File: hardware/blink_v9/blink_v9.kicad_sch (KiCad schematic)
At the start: 121 parts, among them J1 Conn_01x02, J14 Conn_02x16_Odd_Even, J15 Conn_01x01, J16 Conn_01x01, J5 Conn_01x06_Pin, J6 Conn_01x03, J7 Conn_01x06_Pin, J9 USB_C_Receptacle, Q1 S8550, Q2 S8050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

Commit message: add temp sensor
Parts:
- added C30: 100n, Capacitor_SMD:C_0402_1005Metric, symbol Device:C_Small
- added U10: TMP102xxDRL, Package_TO_SOT_SMD:SOT-563, symbol Sensor_Temperature:TMP102xxDRL
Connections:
- net +3.3V: now also C30.2, U10.5 (V+)
- net GND: now also C30.1, U10.2 (GND), U10.4 (ADD0)
- net SDA: now also U10.6 (SDA)
- new net SDL: U10.1 (SCL)
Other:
- note added: "I2C Addr: 0x48 (7bit)"
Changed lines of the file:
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@@
     (stroke (width 0) (type default))
   )
+  (text "I2C Addr: 0x48 (7bit)" (at 360.68 134.62 0)
+    (effects (font (size 1.27 1.27)) (justify left bottom))
+  )
   (text "To iPhone" (at 20.32 184.15 0)
     (effects (font (size 1.27 1.27)) (justify left bottom))
@@
     (effects (font (size 1.27 1.27)) (justify left bottom))
   )
+  (label "SDL" (at 358.14 142.24 180) (fields_autoplaced)
+    (effects (font (size 1.27 1.27)) (justify right bottom))
+  )
   (label "MON_PPS" (at 266.7 46.99 0) (fields_autoplaced)
     (effects (font (size 1.27 1.27)) (justify left bottom))
@@
     (effects (font (size 1.27 1.27)) (justify left bottom))
   )
+  (label "SDA" (at 358.14 139.7 180) (fields_autoplaced)
+    (effects (font (size 1.27 1.27)) (justify right bottom))
+  )
   (global_label "AUX_SYNC_IN" (shape input) (at 287.02 217.17 0) (fields_autoplaced)
     (effects (font (size 1.27 1.27)) (justify left))
@@
     )
   )
+  (symbol (lib_id "Sensor_Temperature:TMP102xxDRL") (at 368.3 144.78 0) (unit 1)
+    (in_bom yes) (on_board yes) (dnp no)
+    (property "Reference" "U10" (at 367.03 144.78 0)
+      (effects (font (size 1.27 1.27)))
+    )
+    (property "Value" "TMP102xxDRL" (at 368.3 154.94 0)
+      (effects (font (size 1.27 1.27)))
+    )
+    (property "Footprint" "Package_TO_SOT_SMD:SOT-563" (at 369.57 153.67 0)
+      (effects (font (size 1.27 1.27)) (justify left) hide)
+    )
+    (property "Datasheet" "https://www.ti.com/lit/ds/symlink/tmp102.pdf" (at 369.57 156.21 0)
+      (effects (font (size 1.27 1.27)) (justify left) hide)
+    )
+    (pin "1")
+    (pin "2")
+    (pin "3")
+    (pin "4")
+    (pin "5")
+    (pin "6")
+    (instances
+      (project "blink_v9"
+        (path "/bd4d3b9a-07c1-4a53-9c94-2893f3e869d4"
+          (reference "U10") (unit 1)
+        )
+      )
+    )
+  )
   (symbol (lib_id "power:GND") (at 163.83 53.34 0) (unit 1)
     (in_bom yes) (on_board yes) (dnp no) (fields_autoplaced)
@@
     )
   )
+  (symbol (lib_id "power:GND") (at 346.71 147.32 0) (unit 1)
+    (in_bom yes) (on_board yes) (dnp no)
+    (property "Reference" "#PWR025" (at 346.71 153.67 0)
+      (effects (font (size 1.27 1.27)) hide)
+    )
+    (property "Value" "GND" (at 346.71 152.4 0)
+      (effects (font (size 1.27 1.27)))
+    )
+    (property "Footprint" "" (at 346.71 147.32 0)
+      (effects (font (size 1.27 1.27)) hide)
+    )
+    (property "Datasheet" "" (at 346.71 147.32 0)
+      (effects (font (size 1.27 1.27)) hide)
+    )
+    (pin "1")
+    (instances
+      (project "blink_v9"
+        (path "/bd4d3b9a-07c1-4a53-9c94-2893f3e869d4"
+          (reference "#PWR025") (unit 1)
+        )
+      )
+    )
+  )
   (symbol (lib_id "power:PWR_FLAG") (at 66.04 45.72 0) (unit 1)
     (in_bom yes) (on_board yes) (dnp no) (fields_autoplaced)
@@
     )
   )
+  (symbol (lib_id "power:+3.3V") (at 368.3 134.62 0) (unit 1)
+    (in_bom yes) (on_board yes) (dnp no) (fields_autoplaced)
+    (property "Reference" "#PWR088" (at 368.3 138.43 0)
+      (effects (font (size 1.27 1.27)) hide)
+    )
+    (property "Value" "+3.3V" (at 368.3 129.54 0)
+      (effects (font (size 1.27 1.27)))
+    )
+    (property "Footprint" "" (at 368.3 134.62 0)
+      (effects (font (size 1.27 1.27)) hide)
+    )
+    (property "Datasheet" "" (at 368.3 134.62 0)
+      (effects (font (size 1.27 1.27)) hide)
+    )
+    (pin "1")
+    (instances
+      (project "blink_v9"
+        (path "/bd4d3b9a-07c1-4a53-9c94-2893f3e869d4"
+          (reference "#PWR088") (unit 1)
+        )
+      )
+    )
+  )
   (symbol (lib_id "power:GND") (at 227.33 219.71 0) (unit 1)
     (in_bom yes) (on_board yes) (dnp no) (fields_autoplaced)
@@
     )
   )
+  (symbol (lib_id "power:GND") (at 368.3 154.94 0) (unit 1)
+    (in_bom yes) (on_board yes) (dnp no)
+    (property "Reference" "#PWR024" (at 368.3 161.29 0)
+      (effects (font (size 1.27 1.27)) hide)
+    )
+    (property "Value" "GND" (at 368.3 160.02 0)
+      (effects (font (size 1.27 1.27)))
+    )
+    (property "Footprint" "" (at 368.3 154.94 0)
+      (effects (font (size 1.27 1.27)) hide)
+    )
+    (property "Datasheet" "" (at 368.3 154.94 0)
+      (effects (font (size 1.27 1.27)) hide)
+    )
+    (pin "1")
+    (instances
+      (project "blink_v9"
+        (path "/bd4d3b9a-07c1-4a53-9c94-2893f3e869d4"
+          (reference "#PWR024") (unit 1)
+        )
+      )
+    )
+  )
   (symbol (lib_id "Mechanical:MountingHole") (at 118.11 54.61 0) (unit 1)
     (in_bom no) (on_board yes) (dnp yes) (fields_autoplaced)
@@
     )
   )
+  (symbol (lib_id "power:GND") (at 358.14 147.32 0) (unit 1)
+    (in_bom yes) (on_board yes) (dnp no)
+    (property "Reference" "#PWR090" (at 358.14 153.67 0)
+      (effects (font (size 1.27 1.27)) hide)
+    )
+    (property "Value" "GND" (at 358.14 152.4 0)
+      (effects (font (size 1.27 1.27)))
+    )
+    (property "Footprint" "" (at 358.14 147.32 0)
+      (effects (font (size 1.27 1.27)) hide)
+    )
+    (property "Datasheet" "" (at 358.14 147.32 0)
+      (effects (font (size 1.27 1.27)) hide)
+    )
+    (pin "1")
+    (instances
+      (project "blink_v9"
+        (path "/bd4d3b9a-07c1-4a53-9c94-2893f3e869d4"
+          (reference "#PWR090") (unit 1)
+        )
+      )
+    )
+  )
   (symbol (lib_id "power:+3.3VA") (at 300.99 96.52 0) (unit 1)
     (in_bom yes) (on_board yes) (dnp no) (fields_autoplaced)
@@
     )
   )
+  (symbol (lib_id "power:+3.3V") (at 346.71 142.24 0) (unit 1)
+    (in_bom yes) (on_board yes) (dnp no) (fields_autoplaced)
+    (property "Reference" "#PWR089" (at 346.71 146.05 0)
+      (effects (font (size 1.27 1.27)) hide)
+    )
+    (property "Value" "+3.3V" (at 346.71 137.16 0)
+      (effects (font (size 1.27 1.27)))
+    )
+    (property "Footprint" "" (at 346.71 142.24 0)
+      (effects (font (size 1.27 1.27)) hide)
+    )
+    (property "Datasheet" "" (at 346.71 142.24 0)
+      (effects (font (size 1.27 1.27)) hide)
+    )
+    (pin "1")
+    (instances
+      (project "blink_v9"
+        (path "/bd4d3b9a-07c1-4a53-9c94-2893f3e869d4"
+          (reference "#PWR089") (unit 1)
+        )
+      )
+    )
+  )
   (symbol (lib_id "Interface_USB:CH340C") (at 330.2 189.23 0) (mirror y) (unit 1)
     (in_bom yes) (on_board yes) (dnp no)
@@
         )
       )
+    )
+  )
+  (symbol (lib_id "Device:C_Small") (at 346.71 144.78 180) (unit 1)
+    (in_bom yes) (on_board yes) (dnp no) (fields_autoplaced)
+    (property "Reference" "C30" (at 349.25 143.5036 0)
+      (effects (font (size 1.27 1.27)) (justify right))
+    )
+    (property "Value" "100n" (at 349.25 146.0436 0)
+      (effects (font (size 1.27 1.27)) (justify right))
+    )
+    (property "Footprint" "Capacitor_SMD:C_0402_1005Metric" (at 346.71 144.78 0)
+      (effects (font (size 1.27 1.27)) hide)
+    )
+    (property "Datasheet" "https://www.mouser.ca/datasheet/2/447/UPY_GPHC_X7R_6_3V_to_250V_23-3084653.pdf" (at 346.71 144.78 0)
+      (effects (font (size 1.27 1.27)) hide)
+    )
+    (property "LCSC" "" (at 346.71 144.78 0)
+      (effects (font (size 1.27 1.27)) hide)
+    )
+    (property "JLCPCB Part #" "C307331" (at 346.71 144.78 0)
+      (effects (font (size 1.27 1.27)) hide)
+    )
+    (pin "1")
+    (pin "2")
+    (instances
+      (project "blink_v9"
+        (path "/bd4d3b9a-07c1-4a53-9c94-2893f3e869d4"
+          (reference "C30") (unit 1)
+        )
+      )

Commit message: fix up osc footprint
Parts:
- Q1, Q2: footprint Package_TO_SOT_SMD:SC-59 -> Package_TO_SOT_THT:TO-92_Inline
- SW2, SW3, SW5: footprint blinky_footprints:LC1258OASP -> Footprints:LC1258OASP
- X1: footprint blinky_footprints:Oscillator_DIP-14 -> blinky_footprints:OSC_DIP-14
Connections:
- net SDL is gone; now on net SCL: U10.1 (SCL)
- no-connect marks 12 -> 13

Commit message: place parts on v9
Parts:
- Q1, Q2: footprint Package_TO_SOT_THT:TO-92_Inline -> Package_TO_SOT_SMD:SOT-23-3
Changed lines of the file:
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@@
       (effects (font (size 1.27 1.27)) (justify left))
     )
-    (property "Footprint" "Package_TO_SOT_THT:TO-92_Inline" (at 328.93 60.325 0)
+    (property "Footprint" "Package_TO_SOT_SMD:SOT-23-3" (at 328.93 60.325 0)
       (effects (font (size 1.27 1.27) italic) (justify left) hide)
     )
@@
       (effects (font (size 1.27 1.27)) (justify left))
     )
-    (property "Footprint" "Package_TO_SOT_THT:TO-92_Inline" (at 330.2 41.275 0)
+    (property "Footprint" "Package_TO_SOT_SMD:SOT-23-3" (at 330.2 41.275 0)
       (effects (font (size 1.27 1.27) italic) (justify left) hide)
     )

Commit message: fix up SMD sizes to motly 0603 on blink
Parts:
- C25: footprint Capacitor_SMD:C_0805_2012Metric -> Capacitor_SMD:C_0603_1608Metric; JLCPCB Part # C14857 -> C1671
- C28, C29: footprint Capacitor_SMD:C_0402_1005Metric -> Capacitor_SMD:C_0603_1608Metric; JLCPCB Part # C23733 -> C19666
- C? (x3): footprint Capacitor_SMD:C_0805_2012Metric -> Capacitor_SMD:C_0603_1608Metric; JLCPCB Part # C49678 -> C14663
- C? (x4): footprint Capacitor_SMD:C_0805_2012Metric -> Capacitor_SMD:C_0603_1608Metric; JLCPCB Part # C15850 -> C19702
- R21, R22: footprint Resistor_SMD:R_0402_1005Metric -> Resistor_SMD:R_0603_1608Metric; JLCPCB Part # C25905 -> C23186
- R24, R25, R35, R36: footprint Resistor_SMD:R_0805_2012Metric -> Resistor_SMD:R_0603_1608Metric; JLCPCB Part # C17540 -> C8218
- R? (x3): footprint Resistor_SMD:R_0805_2012Metric -> Resistor_SMD:R_0603_1608Metric; JLCPCB Part # C17713 -> C25819
- R? (x5): footprint Resistor_SMD:R_0805_2012Metric -> Resistor_SMD:R_0603_1608Metric; JLCPCB Part # C28636 -> C23204
- R?: footprint Resistor_SMD:R_0805_2012Metric -> Resistor_SMD:R_0603_1608Metric; JLCPCB Part # C149504 -> C25803
- R?: footprint Resistor_SMD:R_0805_2012Metric -> Resistor_SMD:R_0603_1608Metric; JLCPCB Part # C25271 -> C22936
- R?: footprint Resistor_SMD:R_0805_2012Metric -> Resistor_SMD:R_0603_1608Metric; JLCPCB Part # C17513 -> C21190
- R?: footprint Resistor_SMD:R_0805_2012Metric -> Resistor_SMD:R_0603_1608Metric; JLCPCB Part # C17414 -> C25804

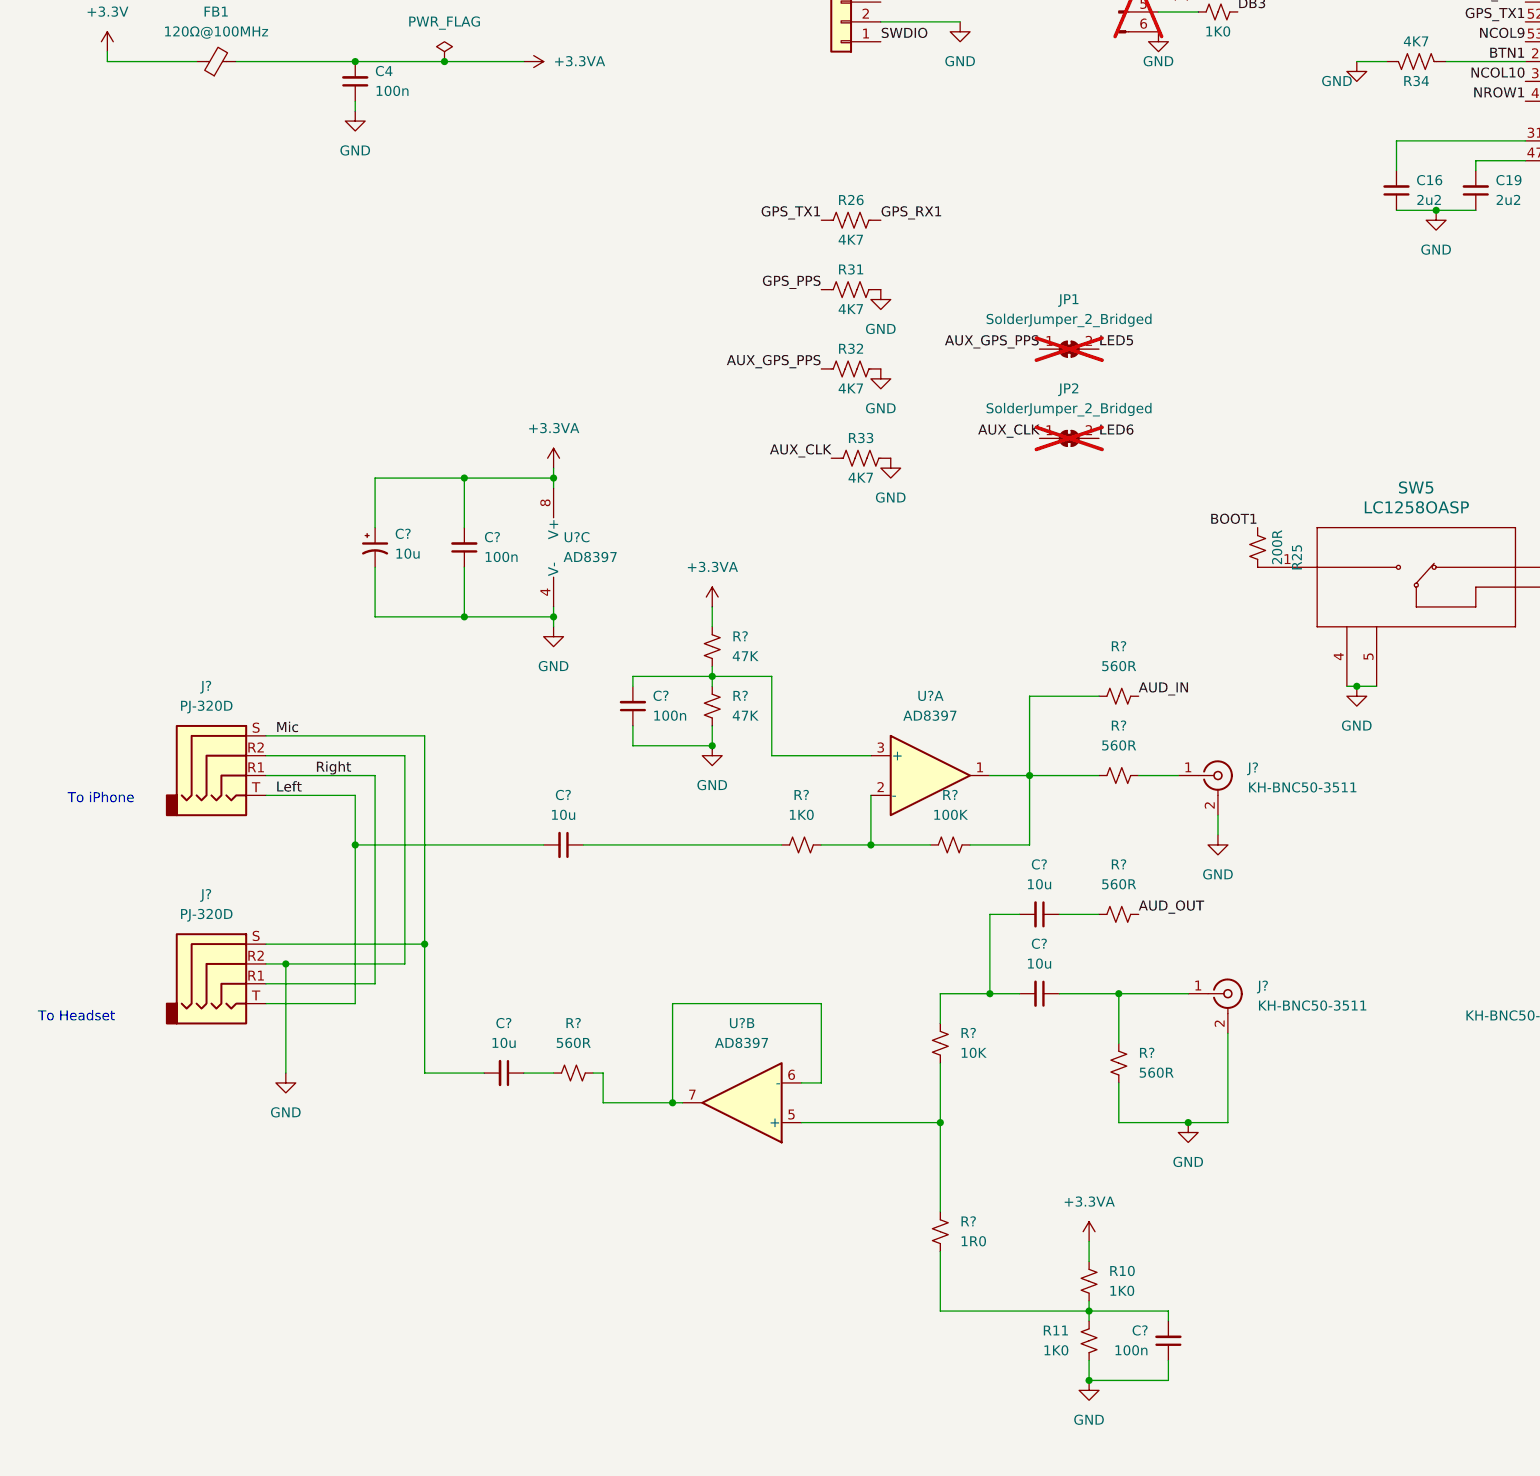
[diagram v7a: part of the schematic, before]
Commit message: add RGB led
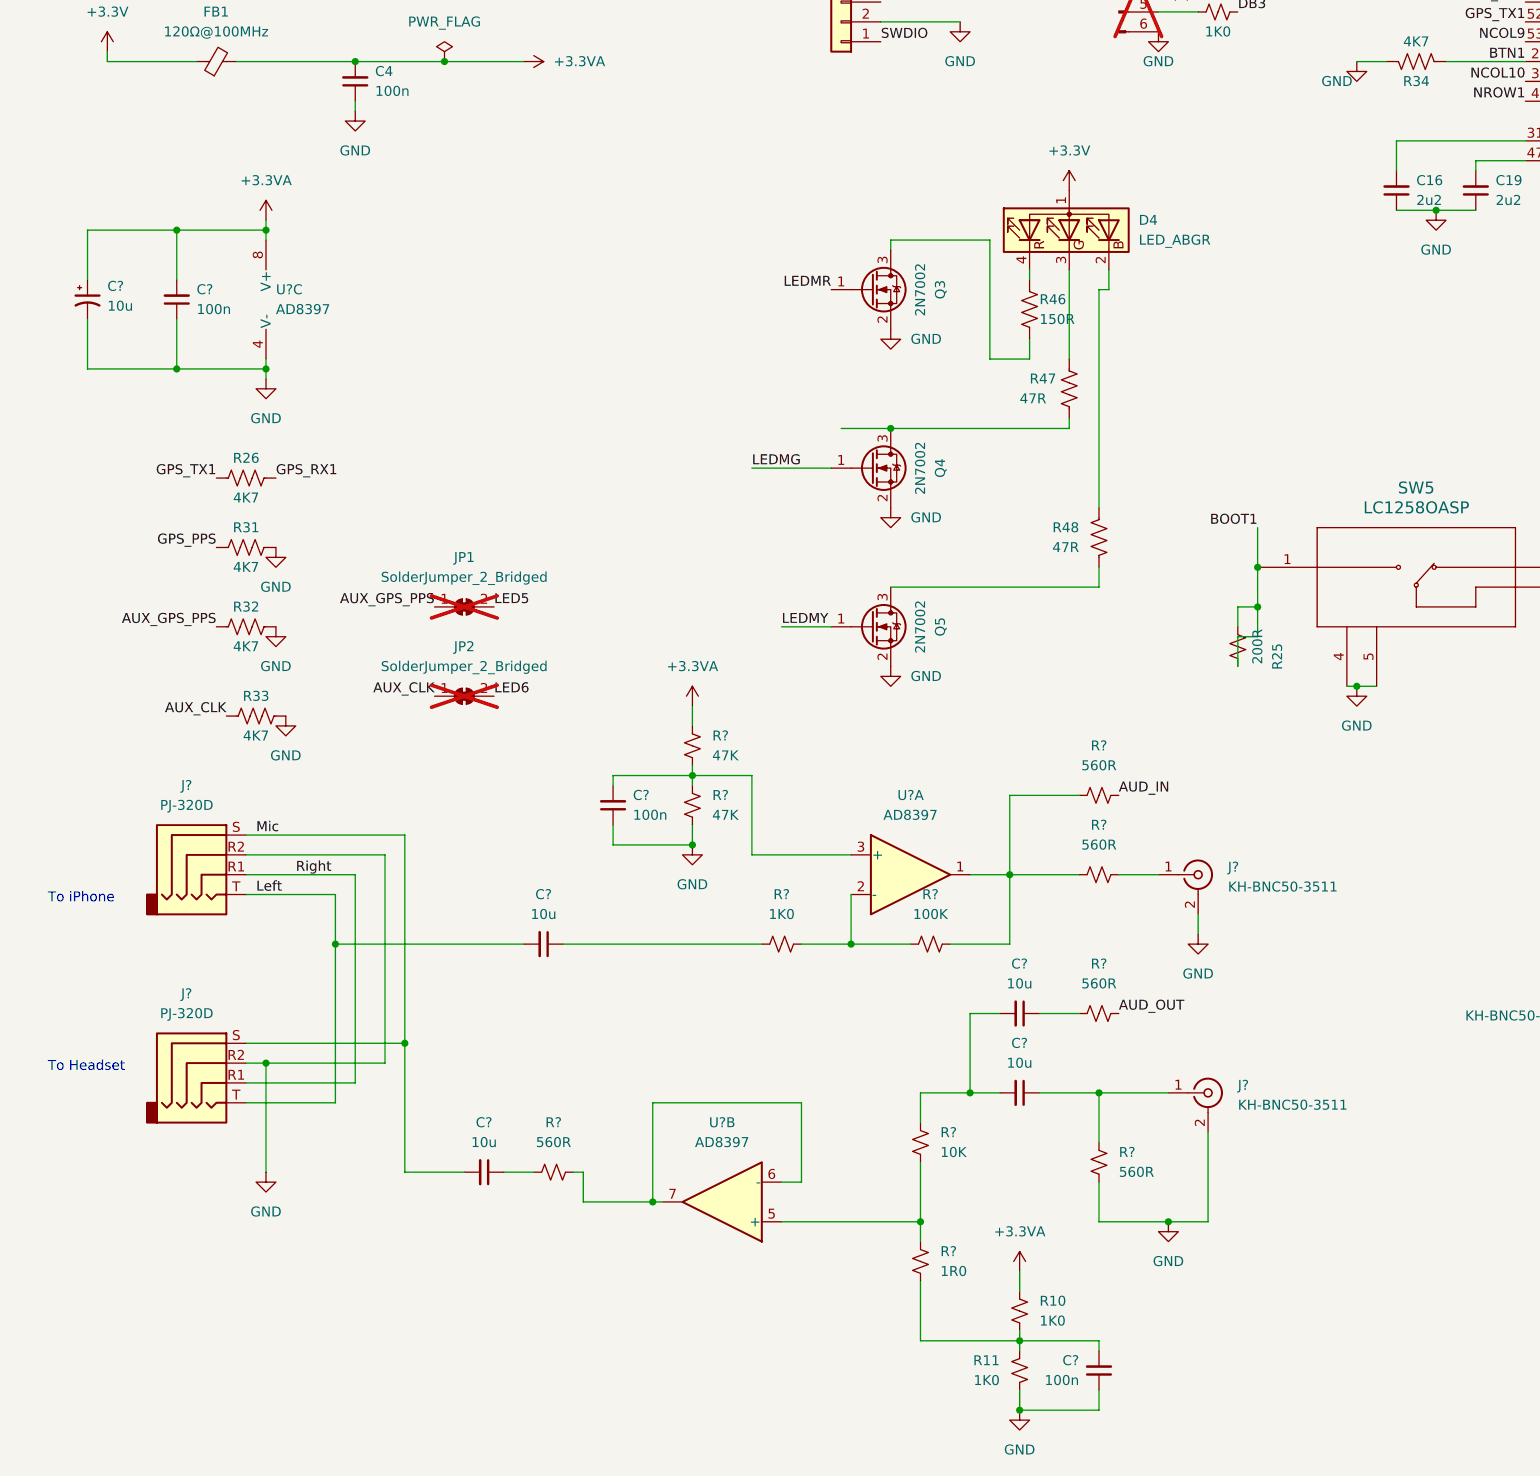
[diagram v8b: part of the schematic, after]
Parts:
- added D4: LED_ABGR, blinky_footprints:LED_RGB_MHS110FRGBCT, symbol Device:LED_ABGR
- added Q3, Q4, Q5: 2N7002, Package_TO_SOT_SMD:SOT-23, symbol Transistor_FET:2N7002
- added R46: 150R, Resistor_SMD:R_0603_1608Metric, symbol Device:R_US
- added R47, R48: 47R, Resistor_SMD:R_0603_1608Metric, symbol Device:R_US
- J6: JLCPCB Part # (none) -> C265101
- U10: JLCPCB Part # (none) -> C99269
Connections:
- net +3.3V: now also D4.1 (A)
- net BOOT1: now also R25.1, SW5.1
- net GND: now also Q3.2 (S), Q4.2 (S), Q5.2 (S)
- net LEDMG: now also Q4.1 (G)
- net LEDMR: now also Q3.1 (G)
- net LEDMY: now also Q5.1 (G)
- new net: Q4.3 (D), R47.1
- new net: D4.2 (BK), R48.1
- new net: Q5.3 (D), R48.2
- new net: D4.3 (GK), R47.2
- new net: D4.4 (RK), R46.2
- new net: Q3.3 (D), R46.1
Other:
- moved on the sheet: C?, J?, JP1, JP2, R10, R11, R25, R26, R31, R32, R33, R?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
